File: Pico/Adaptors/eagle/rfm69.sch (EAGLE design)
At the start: 3 parts

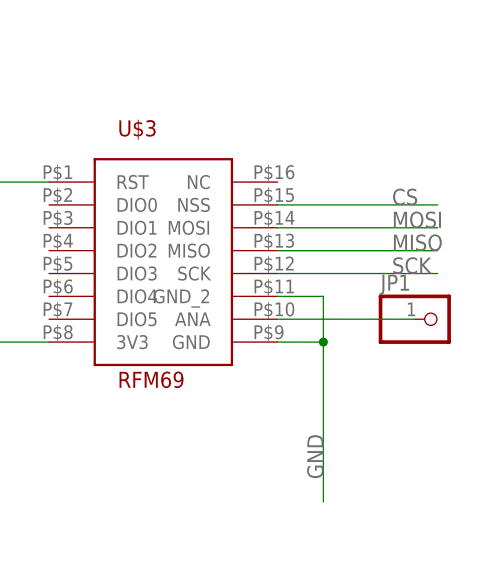
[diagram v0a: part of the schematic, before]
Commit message: added robot shield, and tweaked RFM69 shim (getting protos made)
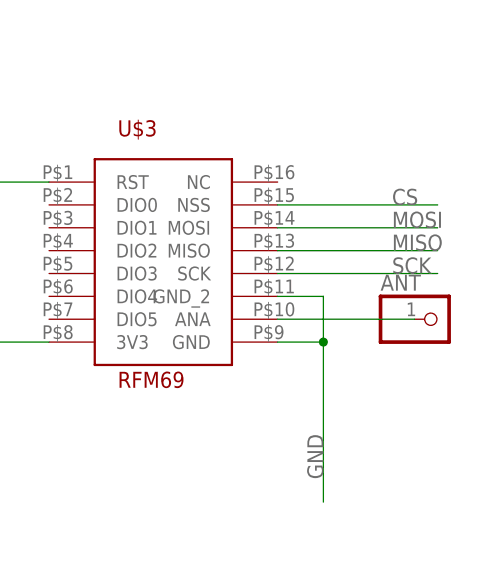
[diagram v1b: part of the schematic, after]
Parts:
- renumbered JP1 to ANT
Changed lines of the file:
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@@
 <parts>
 <part name="U$1" library="espruino_pico" deviceset="ESPRUINO_PICO_SMDONLY" device=""/>
-<part name="JP1" library="pinhead" deviceset="PINHD-1X1" device=""/>
+<part name="ANT" library="pinhead" deviceset="PINHD-1X1" device=""/>
 <part name="U$3" library="RFM69" deviceset="RFM69" device=""/>
 </parts>
@@
 <instances>
 <instance part="U$1" gate="G$1" x="40.64" y="50.8"/>
-<instance part="JP1" gate="G$1" x="139.7" y="35.56"/>
+<instance part="ANT" gate="G$1" x="139.7" y="35.56"/>
 <instance part="U$3" gate="G$1" x="109.22" y="43.18"/>
 </instances>
@@
 <net name="N$1" class="0">
 <segment>
-<pinref part="JP1" gate="G$1" pin="1"/>
+<pinref part="ANT" gate="G$1" pin="1"/>
 <pinref part="U$3" gate="G$1" pin="ANA"/>
 <wire x1="121.92" y1="35.56" x2="137.16" y2="35.56" width="0.1524" layer="91"/>

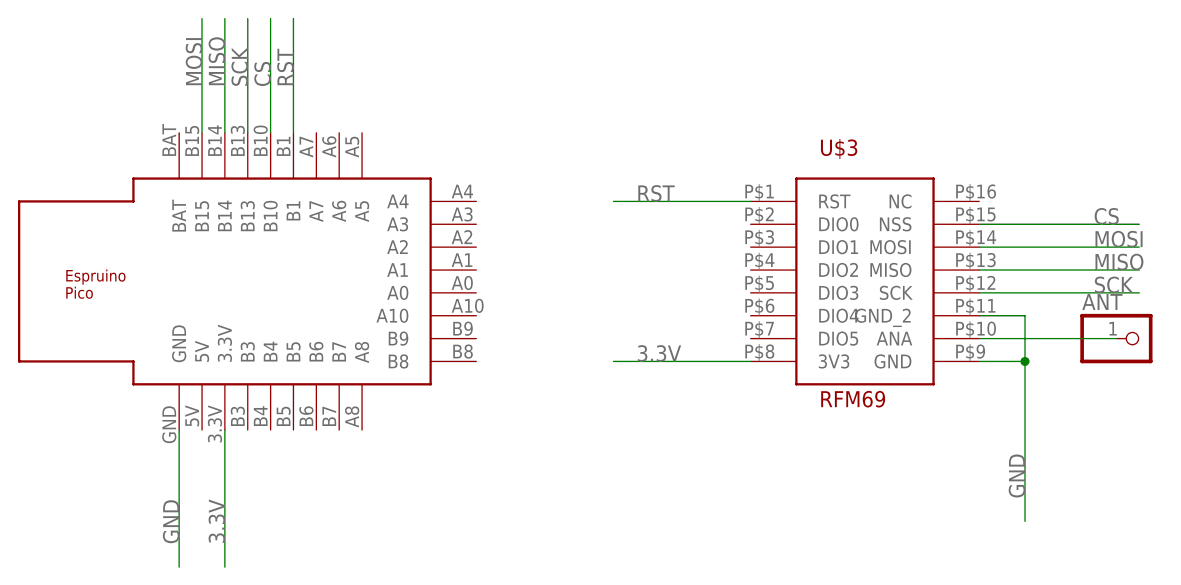
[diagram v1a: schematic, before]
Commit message: add irq line
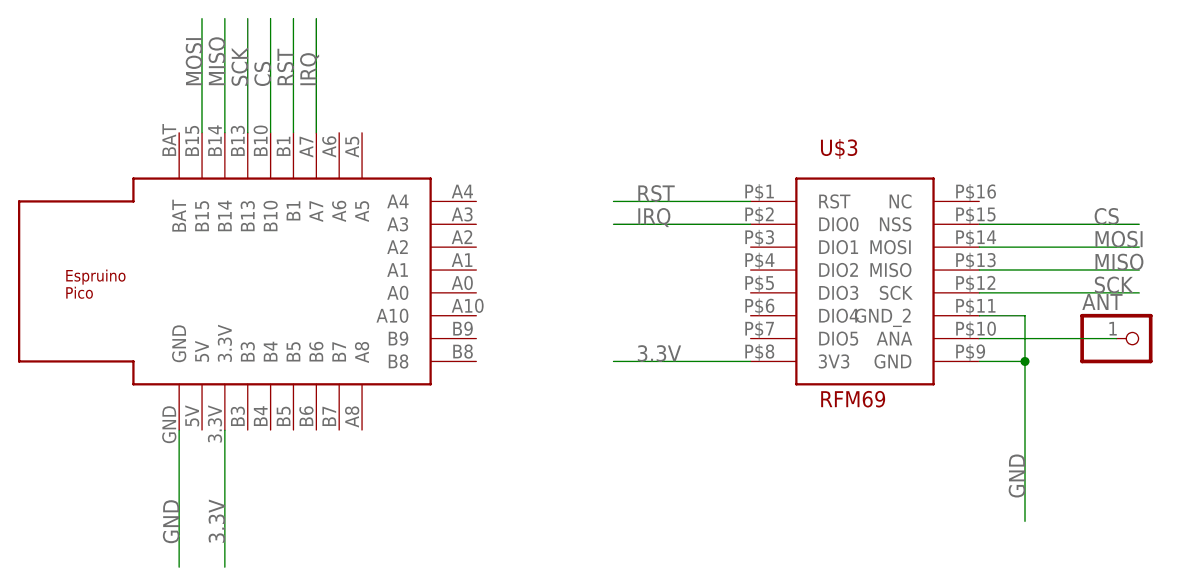
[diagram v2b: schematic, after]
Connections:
- new net IRQ: U$1.A7, U$3.DIO0
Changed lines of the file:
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@@
+</segment>
+</net>
+<net name="IRQ" class="0">
+<segment>
+<pinref part="U$3" gate="G$1" pin="DIO0"/>
+<wire x1="96.52" y1="48.26" x2="81.28" y2="48.26" width="0.1524" layer="91"/>
+<label x="83.82" y="48.26" size="1.778" layer="95"/>
+</segment>
+<segment>
+<pinref part="U$1" gate="G$1" pin="A7"/>
+<wire x1="48.26" y1="58.42" x2="48.26" y2="71.12" width="0.1524" layer="91"/>
+<label x="48.26" y="63.5" size="1.778" layer="95" rot="R90"/>
 </segment>
 </net>
